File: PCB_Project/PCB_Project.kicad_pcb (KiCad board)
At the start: 2 copper layers, 55 x 55 mm, 39 parts, among them J2 ZE27-O3, J3 Motor_Connector, J4 Motor_Connector, J5 Motor_Connector, J6 Motor_Connector, Q1 BSS138, Q2 BSS138, Q3 MMBT2222A, Q4 MMBT2222A

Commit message: working on final board
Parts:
- added C1: 100nF, Capacitor_SMD:C_0402_1005Metric, F.Cu at (56.4, 104.2)
- added C2: 100nF, Capacitor_SMD:C_0402_1005Metric, F.Cu at (56.4, 106.2)
- added U1: ~, Sensor:PQFN50P450X300X100-16N, F.Cu at (97.5, 86.7)
- U11: footprint Sensor:SOIC127P600X175-8N_ADT7410TRZ-REEL -> Sensor:SOIC127P600X175-8N
- U2: footprint Sensor:QFN_BMI085_BOS -> Sensor:PQFN50P450X300X100-16N
- moved C13 86.2 mm to (73.3, 93.6), turned to 0 degrees
- moved R10 79.7 mm to (76.2, 89.7)
- moved C15 74.0 mm to (73.3, 97.5), turned to 0 degrees
- moved R6 72.7 mm to (76.2, 85.7)
- moved R7 72.1 mm to (76.2, 87.7)
- moved C5 69.9 mm to (56.4, 110.1)
- moved C8 68.9 mm to (73.3, 83.7), turned to 0 degrees
- moved C4 68.7 mm to (56.4, 108.2)
- moved C14 67.9 mm to (73.3, 95.5), turned to 0 degrees
- moved R11 62.2 mm to (76.2, 91.7), turned to 0 degrees
- moved C9 59.0 mm to (73.3, 85.7), turned to 0 degrees
- moved R3 58.1 mm to (76.2, 83.7)
- moved R12 49.9 mm to (76.2, 93.7)
- moved R13 49.7 mm to (76.2, 95.7), turned to 0 degrees
- moved C12 48.5 mm to (73.3, 91.6)
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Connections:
- net SDI_1 renamed MOSI_1
- net SDO_1 renamed MISO_1
- U4 pad 10: Pi_RX -> I2C_SCL_M
- U4 pad 12: nCS_2 -> unconnected-(U4-GPIO_18-Pad12)
- U4 pad 26: CSB_Accel_BMI088 -> unconnected-(U4-GPIO_7-Pad26)
- U4 pad 27: I2C_SDA_M -> Pi_TX
- U4 pad 28: I2C_SCL_M -> Pi_RX
- U4 pad 31: unconnected-(U4-GPIO_6-Pad31) -> I2C_SDA_M
- U4 pad 35: SDO_2 -> MISO_2
- U4 pad 36: unconnected-(U4-GPIO_16-Pad36) -> CSB_Accel_BMI088
- U4 pad 38: SDI_2 -> MOSI_2
- U4 pad 40: SCLK_2 -> SCK_2
- U4 pad 8: Pi_TX -> unconnected-(U4-GPIO_14-Pad8)
- U4 pad 9: GND -> unconnected-(U4-GND-Pad9)
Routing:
- net +3V3: track 204.8 -> 0.00 mm, vias 3 -> 0
- net +5V: track 81.4 -> 0.00 mm, vias 1 -> 0
- net I2C_SCL_M: track 68.1 -> 0.00 mm, vias 2 -> 0
- net Pi_RX: track 67.5 -> 0.00 mm, vias 1 -> 0
- net Pi_TX: track 64.6 -> 0.00 mm, vias 1 -> 0
- net I2C_SDA_M: track 63.5 -> 0.00 mm, vias 2 -> 0
- net I2C_SDA_1: track 63.0 -> 8.01 mm, vias 3 -> 0
- net CSB_Accel_BMI088: track 54.6 -> 0.00 mm, vias 1 -> 0
- net I2C_SCL_1: track 63.8 -> 10.3 mm, vias 3 -> 2
- net MISO_1: track 46.1 -> 0.00 mm
- net I2C_SDA_2: track 58.9 -> 17.1 mm, vias 7 -> 0
- net Pi_RX_5V: track 40.5 -> 0.00 mm
- net SCK_1: track 39.8 -> 0.00 mm
- net MOSI_1: track 36.0 -> 0.00 mm, vias 1 -> 0
- net I2C_SCL_M_5V: track 33.4 -> 0.00 mm
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- removed copper zone on B.Cu, net GND
- removed copper zone on F.Cu, net GND
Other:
- board size 55 x 55 mm -> 53 x 50 mm

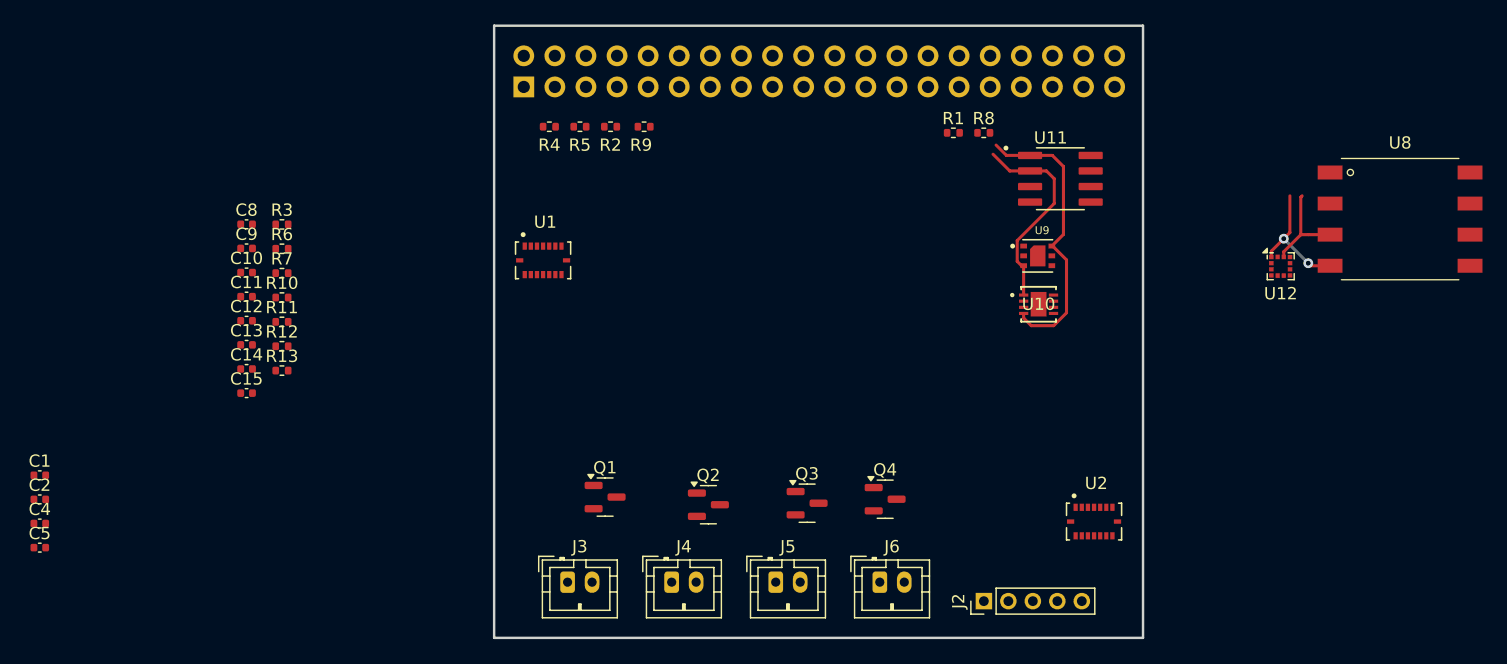
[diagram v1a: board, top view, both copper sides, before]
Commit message: power distribution done
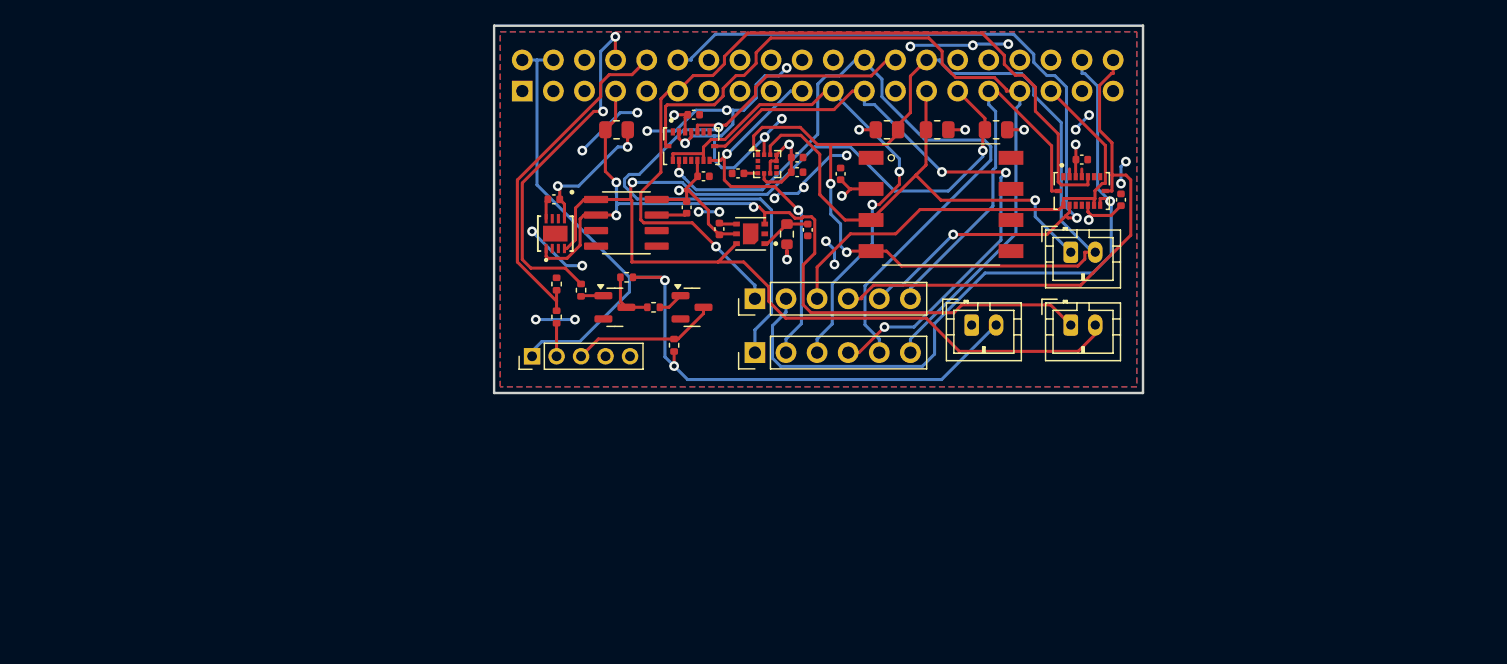
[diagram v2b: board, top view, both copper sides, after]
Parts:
- removed C13, C14, C15: 0.1µF, Capacitor_SMD:C_0402_1005Metric
- removed Q3, Q4: MMBT2222A, Package_TO_SOT_SMD:SOT-23
- removed R10, R11, R13, R6, R7: 1k, Resistor_SMD:R_0402_1005Metric
- removed R12: 2k, Resistor_SMD:R_0402_1005Metric
- removed R8, R9: 5k, Resistor_SMD:R_0402_1005Metric
- removed U10: ~, Sensor:WSON8_DEH_TEX
- removed U11: ~, Sensor:SOIC127P600X175-8N
- removed U12: ~, Package_LGA:LGA-12_2x2mm_P0.5mm
- removed U9: ~, Sensor:XDCR_SGP41-D-R4
- added C3: 1µF, Capacitor_SMD:C_0402_1005Metric, F.Cu at (119.1, 84.2)
- added C6: 0.1µF, Capacitor_SMD:C_0402_1005Metric, F.Cu at (121.8, 79.6)
- added C7: 0.1µF, Capacitor_SMD:C_0402_1005Metric, F.Cu at (109.2, 82.3)
- added J1: Power Connector, Connector_JST:JST_PH_B2B-PH-K_1x02_P2.00mm_Vertical, F.Cu at (132.5, 92.0)
- added R22: 1k, Resistor_SMD:R_0402_1005Metric, F.Cu at (104.3, 88.0)
- added R23: 1k, Resistor_SMD:R_0402_1005Metric, F.Cu at (108.2, 93.6)
- added R24: 1k, Resistor_SMD:R_0402_1005Metric, F.Cu at (106.5, 90.5)
- added R25: 1k, Resistor_SMD:R_0402_1005Metric, F.Cu at (100.6, 89.1)
- added R26: 2k, Resistor_SMD:R_0402_1005Metric, F.Cu at (98.6, 88.6)
- added R27: 1k, Resistor_SMD:R_0402_1005Metric, F.Cu at (98.6, 91.3)
- added U3: ~, Sensor:XDCR_SGP41-D-R4, F.Cu at (114.5, 84.5)
- added U5: ~, Sensor:WSON8_DEH_TEX, F.Cu at (98.5, 84.5)
- added U6: ~, Sensor:SOIC127P600X175-8N, F.Cu at (104.3, 83.6)
- added U7: ~, Sensor:PQFN50P450X300X100-16N, F.Cu at (109.6, 77.3)
- C11: value 1 µF -> 100nF
- C2, C5: value 100nF -> 1µF
- C8: value 1µF -> 0.1µF
- C9: value 1µF -> 100nF
- J3: value Motor_Connector -> i2c1
- J4: value Motor_Connector -> i2c2
- J5: value Motor_Connector -> SPI1; footprint Connector_JST:JST_PH_B2B-PH-K_1x02_P2.00mm_Vertical -> Connector_PinHeader_2.54mm:PinHeader_1x06_P2.54mm_Vertical
- J6: value Motor_Connector -> SPI2; footprint Connector_JST:JST_PH_B2B-PH-K_1x02_P2.00mm_Vertical -> Connector_PinHeader_2.54mm:PinHeader_1x06_P2.54mm_Vertical
- Q1, Q2: value BSS138 -> MMBT2222A
- R1, R2, R4: value 5k -> 1.8k; footprint Resistor_SMD:R_0402_1005Metric -> Resistor_SMD:R_0805_2012Metric
- R3: value 4.7 -> 1.8k; footprint Resistor_SMD:R_0402_1005Metric -> Resistor_SMD:R_0805_2012Metric
- R5: value 5k -> 4.7; footprint Resistor_SMD:R_0402_1005Metric -> Resistor_SMD:R_0603_1608Metric
- U1: footprint Sensor:PQFN50P450X300X100-16N -> Connector_PinSocket_2.54mm:PinSocket_2x20_P2.54mm_Vertical; moved to B.Cu
- U2: footprint Sensor:PQFN50P450X300X100-16N -> Package_LGA:LGA-12_2x2mm_P0.5mm
- U4: footprint Connector_PinSocket_2.54mm:PinSocket_2x20_P2.54mm_Vertical -> Sensor:HNNJ footprint; moved to F.Cu
- U8: footprint Sensor:HNNJ footprint -> Sensor:PQFN50P450X300X100-16N
- moved C12 72.1 mm to (144.7, 81.7), turned to 90 degrees
- moved C10 68.8 mm to (141.5, 78.4)
- moved C2 67.4 mm to (118.2, 79.5)
- moved C1 67.1 mm to (118.2, 78.3)
- moved C4 63.8 mm to (113.4, 79.6), turned to 180 degrees
- moved C5 61.3 mm to (111.9, 84.1), turned to -90 degrees
- moved R3 50.0 mm to (125.6, 76.0)
- moved J3 49.1 mm to (140.6, 86.0)
- moved J2 42.0 mm to (96.6, 94.5)
- moved U2 39.6 mm to (115.8, 78.8)
- moved J4 38.8 mm to (140.6, 92.0)
- moved C11 38.6 mm to (110.6, 79.8)
- moved C9 38.1 mm to (109.8, 74.8)
- moved U4 37.1 mm to (130.0, 87.1), turned to 0 degrees
- moved R4 36.5 mm to (134.5, 76.0), turned to 180 degrees
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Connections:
- C10 pad 1: Net-(U12-C1) -> +3V3
- C4 pad 1: +3V3 -> Net-(U2-C1)
- C5 pad 1: +3V3 -> GND
- C5 pad 2: GND -> +3V3
- C8 pad 1: GND -> +3V3
- C8 pad 2: +3V3 -> GND
- J3 pad 1: I2C_SCL_M_5V -> I2C_SDA_1
- J3 pad 2: I2C_SDA_M_5V -> I2C_SCL_1
- J4 pad 1: I2C_SCL_M_5V -> I2C_SDA_2
- J4 pad 2: I2C_SDA_M_5V -> I2C_SCL_2
- J5 pad 1: I2C_SCL_M_5V -> CSB_Gryo_BMI088_2
- J5 pad 2: I2C_SDA_M_5V -> MOSI_2
- J6 pad 1: I2C_SCL_M_5V -> CSB_Gryo_BMI088_1
- J6 pad 2: I2C_SDA_M_5V -> MOSI_1
- Q1 pad 1: +3V3 -> Net-(Q1-B)
- Q1 pad 2: I2C_SDA_M -> GND
- Q1 pad 3: I2C_SDA_M_5V -> Pi_TX_5V
- Q2 pad 1: +3V3 -> Net-(Q2-B)
- Q2 pad 2: I2C_SCL_M -> GND
- Q2 pad 3: I2C_SCL_M_5V -> Net-(Q2-C)
- R1 pad 2: I2C_SCL_2 -> I2C_SDA_2
- R2 pad 2: I2C_SDA_2 -> I2C_SDA_1
- R3 pad 2: Net-(U9-VDD) -> I2C_SCL_1
- R4 pad 2: I2C_SDA_1 -> I2C_SCL_2
- R5 pad 2: I2C_SCL_1 -> Net-(U3-VDD)
- U1 pad 1: unconnected-(U1-INT2-Pad1) -> +3V3
- U1 pad 10: MISO_2 -> Pi_RX
- U1 pad 11: +3V3 -> CSB_Gryo_BMI088_2
- U1 pad 12: unconnected-(U1-INT3-Pad12) -> CSB_Accel_BMI088_2
- U1 pad 14: CSB_Accel_BMI088 -> GND
- U1 pad 15: MISO_2 -> unconnected-(U1-GPIO_22-Pad15)
- U1 pad 2: GND -> +5V
- U1 pad 3: +3V3 -> unconnected-(U1-GPIO_2-Pad3)
- U1 pad 4: GND -> +5V
- U1 pad 5: CSB_Gryo_BMI088 -> unconnected-(U1-GPIO_3-Pad5)
- U1 pad 7: GND -> I2C_SDA_2
- U1 pad 8: SCK_2 -> Pi_TX
- U1 pad 9: MOSI_2 -> GND
- U2 pad 1: unconnected-(U2-INT2-Pad1) -> I2C_SCL_1
- U2 pad 10: MISO_1 -> +3V3
- U2 pad 11: +3V3 -> I2C_SDA_1
- U2 pad 12: unconnected-(U2-INT3-Pad12) -> GND
- U2 pad 3: +3V3 -> GND
- U2 pad 4: GND -> Net-(U2-C1)
- U2 pad 5: CSB_Gryo_BMI088 -> +3V3
- U2 pad 6: GND -> +3V3
- U2 pad 7: GND -> unconnected-(U2-Int-Pad7)
- U2 pad 8: SCK_1 -> unconnected-(U2-DRDY-Pad8)
- U2 pad 9: MOSI_1 -> +3V3
- U4 pad 1: +3V3 -> GND
- U4 pad 2: +5V -> +3V3
- U4 pad 4: +5V -> I2C_SCL_1
- U4 pad 5: I2C_SCL_1 -> unconnected-(U4-N/C-Pad5)
- U4 pad 6: GND -> unconnected-(U4-N/A-Pad6)
- U4 pad 7: I2C_SDA_2 -> unconnected-(U4-N/A-Pad7)
- U8 pad 1: GND -> unconnected-(U8-INT2-Pad1)
- U8 pad 2: +3V3 -> GND
- U8 pad 3: I2C_SDA_1 -> +3V3
- U8 pad 4: I2C_SCL_1 -> GND
- U8 pad 5: unconnected-(U8-N/C-Pad5) -> CSB_Gryo_BMI088_2
- U8 pad 6: unconnected-(U8-N/A-Pad6) -> GND
- U8 pad 7: unconnected-(U8-N/A-Pad7) -> GND
- U8 pad 8: unconnected-(U8-N/A-Pad8) -> SCK_2
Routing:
- net +5V: track 0.00 -> 78.0 mm, vias 0 -> 2
- net GND: track 0.00 -> 77.4 mm, vias 0 -> 26
- net I2C_SCL_2: track 23.7 -> 99.8 mm, vias 0 -> 2
- net CSB_Gryo_BMI088_2: track 0.00 -> 70.3 mm, vias 0 -> 1
- net I2C_SCL_1: track 10.3 -> 78.4 mm
- net CSB_Accel_BMI088_2: track 0.00 -> 65.9 mm, vias 0 -> 2
- net BMI088_INT1_1: track 0.00 -> 63.0 mm
- net CSB_Accel_BMI088_1: track 0.00 -> 59.3 mm, vias 0 -> 1
- net MOSI_2: track 0.00 -> 57.4 mm, vias 0 -> 1
- net +3V3: track 0.00 -> 55.3 mm, vias 0 -> 12
- net CSB_Gryo_BMI088_1: track 0.00 -> 54.5 mm, vias 0 -> 1
- net I2C_SDA_2: track 17.1 -> 69.7 mm, vias 0 -> 3
- net SCK_1: track 0.00 -> 51.0 mm, vias 0 -> 3
- net SCK_2: track 0.00 -> 43.7 mm
- net MISO_1: track 0.00 -> 43.6 mm, vias 0 -> 2
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- added copper zone on B.Cu, net +3V3
- added copper zone on F.Cu, net GND
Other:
- board size 53 x 50 mm -> 53 x 30 mm

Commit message: Update PCB_Project.kicad_pcb
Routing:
- net Pi_TX: track 29.5 -> 28.7 mm
- net +3V3: track 55.3 -> 55.4 mm, vias 12 -> 18
- net GND: vias 26 -> 32
- added copper zone on In2.Cu, net +3V3
- added copper zone on In1.Cu, net GND
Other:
- copper layers 2 -> 4
- board text added: "Payload Sensor Board"

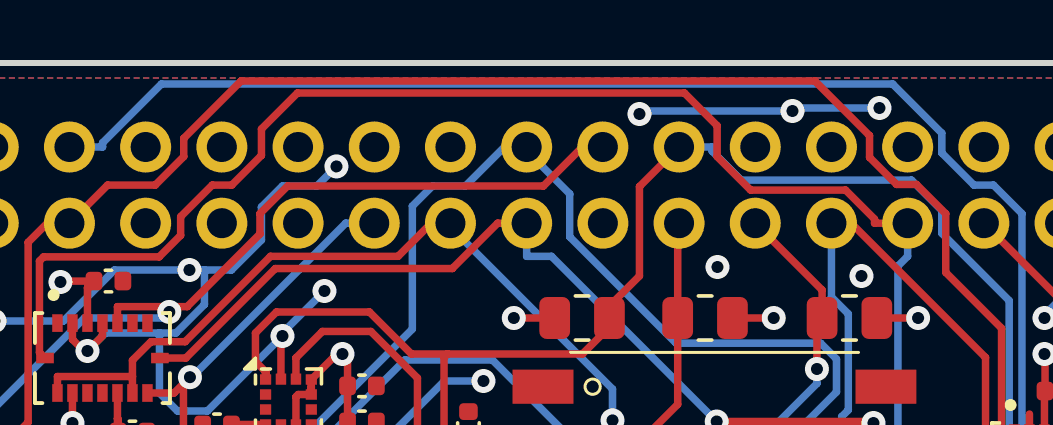
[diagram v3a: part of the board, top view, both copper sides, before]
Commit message: fixed via's
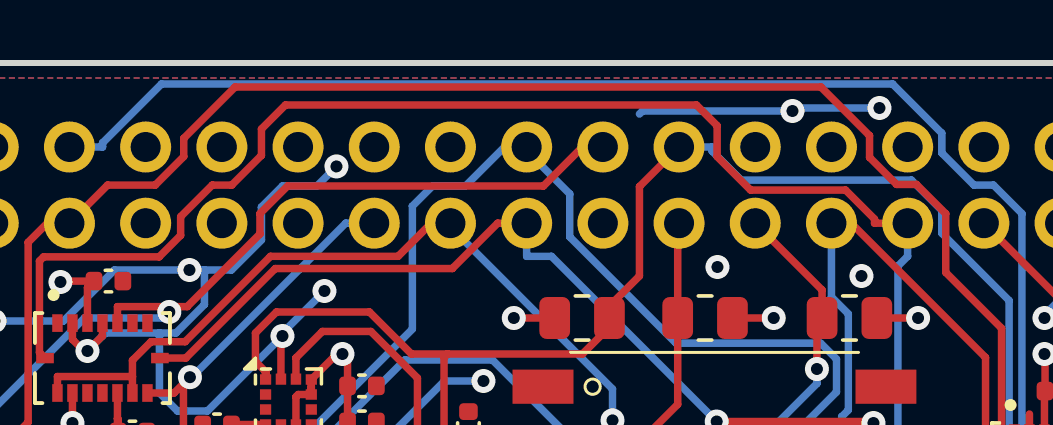
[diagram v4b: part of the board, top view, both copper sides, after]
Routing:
- net GND: vias 32 -> 31
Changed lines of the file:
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@@
 	)
 	(via
-		(at 127.5 69.2)
-		(size 0.8)
-		(drill 0.4)
-		(layers "F.Cu" "B.Cu")
-		(net 3)
-	)
-	(via
 		(at 129 84.9)
 		(size 0.8)
@@
 	)
 	(segment
-		(start 112.207 72.6233)
-		(end 113.26 71.57)
+		(start 113.26 71.57)
+		(end 113.91 71.57)
 		(width 0.25)
 		(layer "F.Cu")
@@
 	)
 	(segment
-		(start 113.26 71.57)
-		(end 113.91 71.57)
+		(start 135.336 72.7019)
+		(end 135.336 72.84)
 		(width 0.25)
 		(layer "F.Cu")
@@
 	)
 	(segment
-		(start 130.09 70.6195)
-		(end 131.207 71.7363)
+		(start 115.7 68.9)
+		(end 129.4 68.9)
 		(width 0.25)
 		(layer "F.Cu")
@@
 	)
 	(segment
-		(start 114.9 69.7)
-		(end 116.1 68.5)
+		(start 135.336 72.84)
+		(end 136.44 72.84)
 		(width 0.25)
 		(layer "F.Cu")
@@
 	)
 	(segment
-		(start 130.09 69.59)
-		(end 130.09 70.6195)
+		(start 107.5 74.1)
+		(end 107.638 73.962)
 		(width 0.25)
 		(layer "F.Cu")
@@
 	)
 	(segment
-		(start 116.1 68.5)
-		(end 129 68.5)
+		(start 114.9 69.7)
+		(end 115.7 68.9)
 		(width 0.25)
 		(layer "F.Cu")
@@
 	)
 	(segment
-		(start 135.336 72.84)
-		(end 136.44 72.84)
+		(start 129.4 68.9)
+		(end 130.09 69.59)
 		(width 0.25)
 		(layer "F.Cu")
@@
 	)
 	(segment
-		(start 134.371 71.7363)
-		(end 135.336 72.7019)
+		(start 107.685 77.335)
+		(end 107.5 77.15)
 		(width 0.25)
 		(layer "F.Cu")
@@
 	)
 	(segment
-		(start 131.207 71.7363)
-		(end 134.371 71.7363)
+		(start 130.09 70.6195)
+		(end 131.207 71.7363)
 		(width 0.25)
 		(layer "F.Cu")
@@
 	)
 	(segment
-		(start 135.336 72.7019)
-		(end 135.336 72.84)
+		(start 112.207 73.2454)
+		(end 112.207 72.6233)
 		(width 0.25)
 		(layer "F.Cu")
@@
 	)
 	(segment
-		(start 129 68.5)
-		(end 130.09 69.59)
+		(start 107.5 77.15)
+		(end 107.5 74.1)
 		(width 0.25)
 		(layer "F.Cu")
@@
 	)
 	(segment
-		(start 107.638 73.962)
-		(end 111.491 73.962)
+		(start 130.09 69.59)
+		(end 130.09 70.6195)
 		(width 0.25)
 		(layer "F.Cu")
@@
 	)
 	(segment
-		(start 113.91 71.57)
-		(end 114.9 70.5801)
+		(start 112.207 72.6233)
+		(end 113.26 71.57)
 		(width 0.25)
 		(layer "F.Cu")
@@
 	)
 	(segment
-		(start 107.5 74.1)
-		(end 107.638 73.962)
+		(start 111.491 73.962)
+		(end 112.207 73.2454)
 		(width 0.25)
 		(layer "F.Cu")
@@
 	)
 	(segment
-		(start 114.9 70.5801)
-		(end 114.9 69.7)
+		(start 134.371 71.7363)
+		(end 135.336 72.7019)
 		(width 0.25)
 		(layer "F.Cu")
@@
 	)
 	(segment
-		(start 107.5 77.15)
-		(end 107.5 74.1)
+		(start 113.91 71.57)
+		(end 114.9 70.5801)
 		(width 0.25)
 		(layer "F.Cu")
@@
 	)
 	(segment
-		(start 111.491 73.962)
-		(end 112.207 73.2454)
+		(start 107.638 73.962)
+		(end 111.491 73.962)
 		(width 0.25)
 		(layer "F.Cu")
@@
 	)
 	(segment
-		(start 107.685 77.335)
-		(end 107.5 77.15)
+		(start 114.9 70.5801)
+		(end 114.9 69.7)
 		(width 0.25)
 		(layer "F.Cu")
@@
 	)
 	(segment
-		(start 112.207 73.2454)
-		(end 112.207 72.6233)
+		(start 131.207 71.7363)
+		(end 134.371 71.7363)
 		(width 0.25)
 		(layer "F.Cu")
@@
 	)
 	(segment
+		(start 139.571 76.3424)
+		(end 137.71 74.4811)
+		(width 0.25)
+		(layer "F.Cu")
+		(net 32)
+	)
+	(segment
 		(start 105.475 81.1251)
 		(end 105.475 83.3486)
@@
 	)
 	(segment
-		(start 139.571 76.3424)
-		(end 137.71 74.4811)
+		(start 136.072 71.5478)
+		(end 135.17 70.6455)
 		(width 0.25)
 		(layer "F.Cu")
@@
 	)
 	(segment
-		(start 137.71 72.5233)
-		(end 136.734 71.5478)
+		(start 137.71 74.4811)
+		(end 137.71 72.5233)
 		(width 0.25)
 		(layer "F.Cu")
@@
 	)
 	(segment
-		(start 139.818 80.5)
-		(end 139.571 80.2535)
+		(start 133.5483 68.3)
+		(end 114.0215 68.3)
 		(width 0.25)
 		(layer "F.Cu")
@@
 	)
 	(segment
-		(start 133.348 68.1)
-		(end 114.222 68.1)
+		(start 136.734 71.5478)
+		(end 136.072 71.5478)
 		(width 0.25)
 		(layer "F.Cu")
@@
 	)
 	(segment
-		(start 136.072 71.5478)
-		(end 135.17 70.6455)
+		(start 112.31 70.0115)
+		(end 112.31 70.6195)
 		(width 0.25)
 		(layer "F.Cu")
@@
 	)
 	(segment
-		(start 136.734 71.5478)
-		(end 136.072 71.5478)
+		(start 135.17 69.9217)
+		(end 133.5483 68.3)
 		(width 0.25)
 		(layer "F.Cu")
@@
 	)
 	(segment
-		(start 137.71 74.4811)
-		(end 137.71 72.5233)
+		(start 109.77 71.57)
+		(end 108.5 72.84)
 		(width 0.25)
 		(layer "F.Cu")
@@
 	)
 	(segment
-		(start 112.31 70.0115)
-		(end 112.31 70.6195)
+		(start 135.17 70.6455)
+		(end 135.17 69.9217)
 		(width 0.25)
 		(layer "F.Cu")
@@
 	)
 	(segment
-		(start 109.77 71.57)
-		(end 108.5 72.84)
+		(start 112.31 70.6195)
+		(end 111.36 71.57)
 		(width 0.25)
 		(layer "F.Cu")
@@
 	)
 	(segment
-		(start 111.36 71.57)
-		(end 109.77 71.57)
+		(start 139.818 80.5)
+		(end 139.571 80.2535)
 		(width 0.25)
 		(layer "F.Cu")
@@
 	)
 	(segment
-		(start 112.31 70.6195)
-		(end 111.36 71.57)
+		(start 137.71 72.5233)
+		(end 136.734 71.5478)
 		(width 0.25)
 		(layer "F.Cu")
@@
 	)
 	(segment
-		(start 142 79.835)
-		(end 142 80.5)
+		(start 111.36 71.57)
+		(end 109.77 71.57)
 		(width 0.25)
 		(layer "F.Cu")
@@
 	)
 	(segment
-		(start 135.17 70.6455)
-		(end 135.17 69.9217)
+		(start 142 79.835)
+		(end 142 80.5)
 		(width 0.25)
 		(layer "F.Cu")
@@
 	)
 	(segment
-		(start 135.17 69.9217)
-		(end 133.348 68.1)
+		(start 139.571 80.2535)
+		(end 139.571 76.3424)
 		(width 0.25)
 		(layer "F.Cu")
@@
 	)
 	(segment
+		(start 114.0215 68.3)
+		(end 112.31 70.0115)
+		(width 0.25)
+		(layer "F.Cu")
+		(net 32)
+	)
+	(segment
 		(start 105.475 83.3486)
 		(end 105.726 83.6)
@@
 		(width 0.25)
 		(layer "F.Cu")
-		(net 32)
-	)
-	(segment
-		(start 139.571 80.2535)
-		(end 139.571 76.3424)
-		(width 0.25)
-		(layer "F.Cu")
-		(net 32)
-	)
-	(segment
-		(start 114.222 68.1)
-		(end 112.31 70.0115)
-		(width 0.25)
-		(layer "F.Cu")
